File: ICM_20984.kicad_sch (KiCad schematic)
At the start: 17 parts, among them Q2 BSS138, Q5 BSS138, U10 ICM-42688-P, U11 LIS3MDL, U13 MIC5365-3.3YC5

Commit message: Rev 2 finished
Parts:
- C23, C24, C44: LCSC Part # C1525 -> C307331
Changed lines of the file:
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@@
 			)
 		)
-		(property "LCSC Part #" "C1525"
+		(property "LCSC Part #" "C307331"
 			(at 50.292 137.16 0)
 			(effects
@@
 			)
 		)
-		(property "LCSC Part #" "C1525"
+		(property "LCSC Part #" "C307331"
 			(at 207.264 118.872 0)
 			(effects
@@
 			)
 		)
-		(property "LCSC Part #" "C1525"
+		(property "LCSC Part #" "C307331"
 			(at 257.81 142.24 0)
 			(effects

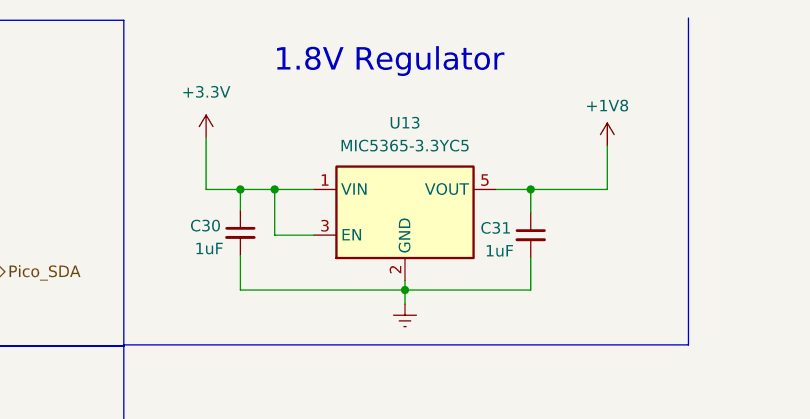
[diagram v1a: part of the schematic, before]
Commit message: Rev 3: fixing I2C and footprints
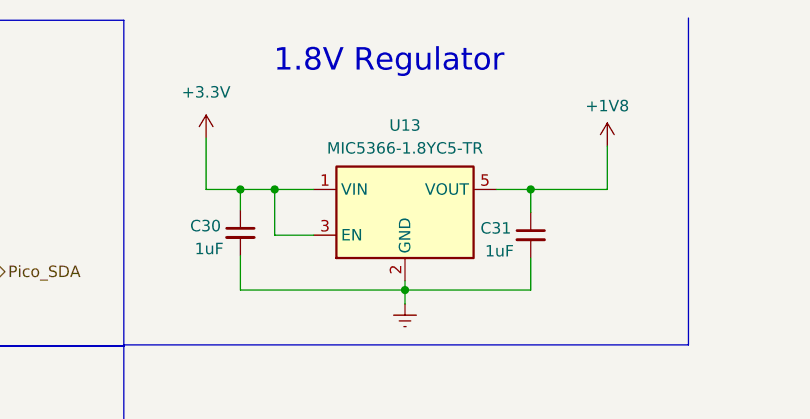
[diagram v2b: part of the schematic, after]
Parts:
- C23, C24, C44: LCSC Part # C307331 -> C1525
- U13: value MIC5365-3.3YC5 -> MIC5366-1.8YC5-TR
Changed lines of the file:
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@@
 		(fields_autoplaced yes)
 		(property "Reference" "U13"
-			(at 103.886 23.876 0)
-			(effects
-				(font
-					(size 1.27 1.27)
-				)
-			)
-		)
-		(property "Value" "MIC5365-3.3YC5"
-			(at 103.886 26.416 0)
+			(at 103.886 24.13 0)
+			(effects
+				(font
+					(size 1.27 1.27)
+				)
+			)
+		)
+		(property "Value" "MIC5366-1.8YC5-TR"
+			(at 103.886 26.67 0)
 			(effects
 				(font
@@
 			)
 		)
-		(property "LCSC Part #" "C307331"
+		(property "LCSC Part #" "C1525"
 			(at 50.292 137.16 0)
 			(effects
@@
 			)
 		)
-		(property "LCSC Part #" "C307331"
+		(property "LCSC Part #" "C1525"
 			(at 207.264 118.872 0)
 			(effects
@@
 			)
 		)
-		(property "LCSC Part #" "C307331"
+		(property "LCSC Part #" "C1525"
 			(at 257.81 142.24 0)
 			(effects

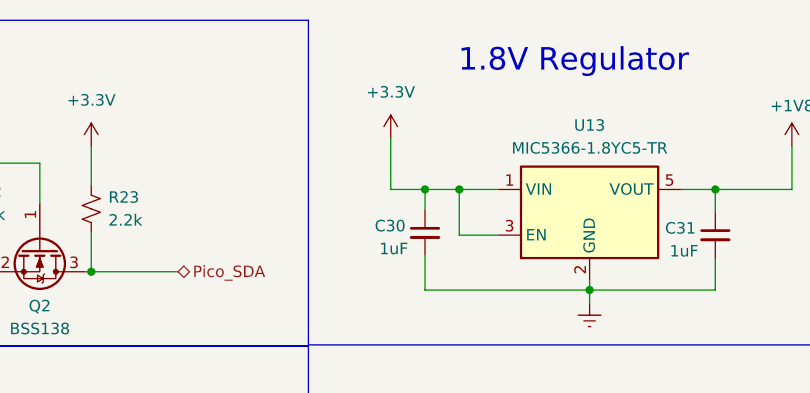
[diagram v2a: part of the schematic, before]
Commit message: Layout for 80x80mm done
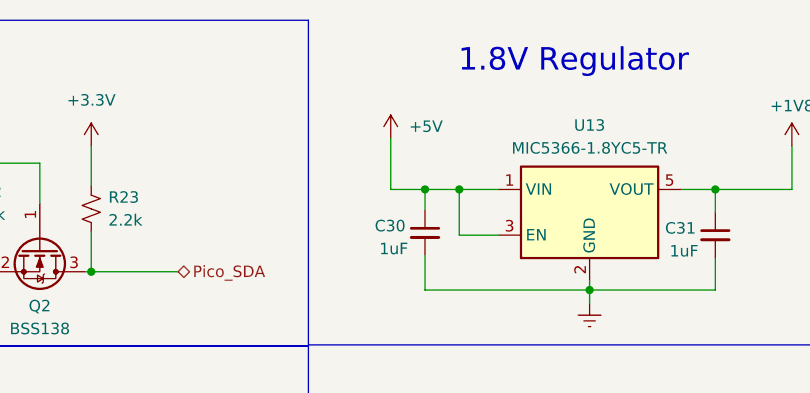
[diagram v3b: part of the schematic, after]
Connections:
- net +3.3V: no longer C30.1, U13.1 (VIN), U13.3 (EN)
- new net +5V: C30.1, U13.1 (VIN), U13.3 (EN)
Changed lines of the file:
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@@
 			)
 		)
-		(property "Value" "+3.3V"
-			(at 81.788 20.447 0)
+		(property "Value" "+5V"
+			(at 83.82 24.2569 0)
 			(effects
 				(font
 					(size 1.27 1.27)
 				)
+				(justify left)
 			)
 		)

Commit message: Graphics
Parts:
- renumbered C30 to C11, C29 to C18, C24 to C22, C31 to C23, C43 to C24, C45 to C25, C23 to C29, C44 to C31, Q5 to Q1, R33 to R15, R22 to R16, R23 to R19, R34 to R20, U11 to U3, U10 to U4, U13 to U5
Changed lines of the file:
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@@
 		(dnp no)
 		(fields_autoplaced yes)
-		(property "Reference" "U13"
+		(property "Reference" "U5"
 			(at 103.886 24.13 0)
 			(effects
@@
 			(project "DeltaRhoRobot"
 				(path "/cced1a6d-3dc4-42b2-93bd-998a7b4cf4e8/ff44b13b-7cc8-487d-9bdf-cc68eec5ba2f/b72e047d-6874-46de-bfdb-cff5124484f7"
-					(reference "U13")
+					(reference "U5")
 					(unit 1)
 				)
@@
 		(on_board yes)
 		(dnp no)
-		(property "Reference" "C30"
+		(property "Reference" "C11"
 			(at 80.01 35.306 0)
 			(effects
@@
 			(project "DeltaRhoRobot"
 				(path "/cced1a6d-3dc4-42b2-93bd-998a7b4cf4e8/ff44b13b-7cc8-487d-9bdf-cc68eec5ba2f/b72e047d-6874-46de-bfdb-cff5124484f7"
-					(reference "C30")
+					(reference "C11")
 					(unit 1)
 				)
@@
 		(dnp no)
 		(fields_autoplaced yes)
-		(property "Reference" "C43"
+		(property "Reference" "C24"
 			(at 36.195 135.8963 0)
 			(effects
@@
 			(project "DeltaRhoRobot"
 				(path "/cced1a6d-3dc4-42b2-93bd-998a7b4cf4e8/ff44b13b-7cc8-487d-9bdf-cc68eec5ba2f/b72e047d-6874-46de-bfdb-cff5124484f7"
-					(reference "C43")
+					(reference "C24")
 					(unit 1)
 				)
@@
 		(on_board yes)
 		(dnp no)
-		(property "Reference" "U11"
+		(property "Reference" "U3"
 			(at 232.664 119.888 0)
 			(effects
@@
 			(project "DeltaRhoRobot"
 				(path "/cced1a6d-3dc4-42b2-93bd-998a7b4cf4e8/ff44b13b-7cc8-487d-9bdf-cc68eec5ba2f/b72e047d-6874-46de-bfdb-cff5124484f7"
-					(reference "U11")
+					(reference "U3")
 					(unit 1)
 				)
@@
 		(dnp no)
 		(fields_autoplaced yes)
-		(property "Reference" "R23"
+		(property "Reference" "R19"
 			(at 50.419 32.131 0)
 			(effects
@@
 			(project "DeltaRhoRobot"
 				(path "/cced1a6d-3dc4-42b2-93bd-998a7b4cf4e8/ff44b13b-7cc8-487d-9bdf-cc68eec5ba2f/b72e047d-6874-46de-bfdb-cff5124484f7"
-					(reference "R23")
+					(reference "R19")
 					(unit 1)
 				)
@@
 		(dnp no)
 		(fields_autoplaced yes)
-		(property "Reference" "C23"
+		(property "Reference" "C29"
 			(at 47.117 135.8963 0)
 			(effects
@@
 			(project "DeltaRhoRobot"
 				(path "/cced1a6d-3dc4-42b2-93bd-998a7b4cf4e8/ff44b13b-7cc8-487d-9bdf-cc68eec5ba2f/b72e047d-6874-46de-bfdb-cff5124484f7"
-					(reference "C23")
+					(reference "C29")
 					(unit 1)
 				)
@@
 		(dnp no)
 		(fields_autoplaced yes)
-		(property "Reference" "C44"
+		(property "Reference" "C31"
 			(at 204.089 117.6083 0)
 			(effects
@@
 			(project "DeltaRhoRobot"
 				(path "/cced1a6d-3dc4-42b2-93bd-998a7b4cf4e8/ff44b13b-7cc8-487d-9bdf-cc68eec5ba2f/b72e047d-6874-46de-bfdb-cff5124484f7"
-					(reference "C44")
+					(reference "C31")
 					(unit 1)
 				)
@@
 		(dnp no)
 		(fields_autoplaced yes)
-		(property "Reference" "R22"
+		(property "Reference" "R16"
 			(at 35.179 31.496 0)
 			(effects
@@
 			(project "DeltaRhoRobot"
 				(path "/cced1a6d-3dc4-42b2-93bd-998a7b4cf4e8/ff44b13b-7cc8-487d-9bdf-cc68eec5ba2f/b72e047d-6874-46de-bfdb-cff5124484f7"
-					(reference "R22")
+					(reference "R16")
 					(unit 1)
 				)
@@
 		(dnp no)
 		(fields_autoplaced yes)
-		(property "Reference" "C24"
+		(property "Reference" "C22"
 			(at 260.985 140.9763 0)
 			(effects
@@
 			(project "DeltaRhoRobot"
 				(path "/cced1a6d-3dc4-42b2-93bd-998a7b4cf4e8/ff44b13b-7cc8-487d-9bdf-cc68eec5ba2f/b72e047d-6874-46de-bfdb-cff5124484f7"
-					(reference "C24")
+					(reference "C22")
 					(unit 1)
 				)
@@
 		(dnp no)
 		(fields_autoplaced yes)
-		(property "Reference" "R34"
+		(property "Reference" "R20"
 			(at 50.419 68.326 0)
 			(effects
@@
 			(project "DeltaRhoRobot"
 				(path "/cced1a6d-3dc4-42b2-93bd-998a7b4cf4e8/ff44b13b-7cc8-487d-9bdf-cc68eec5ba2f/b72e047d-6874-46de-bfdb-cff5124484f7"
-					(reference "R34")
+					(reference "R20")
 					(unit 1)
 				)
@@
 		(on_board yes)
 		(dnp no)
-		(property "Reference" "C45"
+		(property "Reference" "C25"
 			(at 214.376 117.5956 0)
 			(effects
@@
 			(project "DeltaRhoRobot"
 				(path "/cced1a6d-3dc4-42b2-93bd-998a7b4cf4e8/ff44b13b-7cc8-487d-9bdf-cc68eec5ba2f/b72e047d-6874-46de-bfdb-cff5124484f7"
-					(reference "C45")
+					(reference "C25")
 					(unit 1)
 				)
@@
 		(dnp no)
 		(fields_autoplaced yes)
-		(property "Reference" "Q5"
+		(property "Reference" "Q1"
 			(at 42.799 80.391 90)
 			(effects
@@
 			(project "DeltaRhoRobot"
 				(path "/cced1a6d-3dc4-42b2-93bd-998a7b4cf4e8/ff44b13b-7cc8-487d-9bdf-cc68eec5ba2f/b72e047d-6874-46de-bfdb-cff5124484f7"
-					(reference "Q5")
+					(reference "Q1")
 					(unit 1)
 				)
@@
 		(on_board yes)
 		(dnp no)
-		(property "Reference" "U10"
+		(property "Reference" "U4"
 			(at 98.044 122.174 0)
 			(effects
@@
 			(project "DeltaRhoRobot"
 				(path "/cced1a6d-3dc4-42b2-93bd-998a7b4cf4e8/ff44b13b-7cc8-487d-9bdf-cc68eec5ba2f/b72e047d-6874-46de-bfdb-cff5124484f7"
-					(reference "U10")
+					(reference "U4")
 					(unit 1)
 				)
@@
 		(dnp no)
 		(fields_autoplaced yes)
-		(property "Reference" "R33"
+		(property "Reference" "R15"
 			(at 35.179 67.691 0)
 			(effects
@@
 			(project "DeltaRhoRobot"
 				(path "/cced1a6d-3dc4-42b2-93bd-998a7b4cf4e8/ff44b13b-7cc8-487d-9bdf-cc68eec5ba2f/b72e047d-6874-46de-bfdb-cff5124484f7"
-					(reference "R33")
+					(reference "R15")
 					(unit 1)
 				)
@@
 		(on_board yes)
 		(dnp no)
-		(property "Reference" "C31"
+		(property "Reference" "C23"
 			(at 112.268 35.56 0)
 			(effects
@@
 			(project "DeltaRhoRobot"
 				(path "/cced1a6d-3dc4-42b2-93bd-998a7b4cf4e8/ff44b13b-7cc8-487d-9bdf-cc68eec5ba2f/b72e047d-6874-46de-bfdb-cff5124484f7"
-					(reference "C31")
+					(reference "C23")
 					(unit 1)
 				)
@@
 		(on_board yes)
 		(dnp no)
-		(property "Reference" "C29"
+		(property "Reference" "C18"
 			(at 57.404 136.1376 0)
 			(effects
@@
 			(project "DeltaRhoRobot"
 				(path "/cced1a6d-3dc4-42b2-93bd-998a7b4cf4e8/ff44b13b-7cc8-487d-9bdf-cc68eec5ba2f/b72e047d-6874-46de-bfdb-cff5124484f7"
-					(reference "C29")
-					(unit 1)
-				)
+					(reference "C18")
+					(unit 1)
+				)

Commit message: Final
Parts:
- C22, C29, C31: LCSC Part # C1525 -> C307331
- U3: JLCPCB Rotation Offset 90 -> 0
- U4: JLCPCB Rotation Offset (none) -> 0
